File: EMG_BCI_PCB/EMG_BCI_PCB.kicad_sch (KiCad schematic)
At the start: 3 parts, among them J1 Conn_01x03, J2 Conn_01x02, J3 Conn_01x03_Male

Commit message: More schematic changes
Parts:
- removed J1: Conn_01x03, Connector_JST:JST_VH_B3P-VH_1x03_P3.96mm_Vertical, symbol Connector_Generic:Conn_01x03
- removed J2: Conn_01x02, Connector_JST:JST_XH_B2B-XH-AM_1x02_P2.50mm_Vertical, symbol Connector_Generic:Conn_01x02
- removed J3: Conn_01x03_Male, Connector_PinHeader_2.54mm:PinHeader_1x03_P2.54mm_Vertical, symbol Connector:Conn_01x03_Male
- added J1: Conn_01x08_Pin, symbol Connector:Conn_01x08_Pin
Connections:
- net EMG_FrontEnd/Trode+: now also J1.1 (Pin_1)
- net EMG_FrontEnd/Trode-: now also J1.2 (Pin_2)
- net Power/Vin+: now also J1.3 (Pin_3)
- new net Power/RTN: J1.4 (Pin_4)
- new net SpiClk: J1.5 (Pin_5)
- new net SpiCs: J1.8 (Pin_8)
- new net SpiDin: J1.6 (Pin_6)
- new net SpiDout: J1.7 (Pin_7)
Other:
- sheet EMG_Rect renamed EMG_Offset_And_Rect
- sheet EMG_ADC ports: added AdcCh0, AdcCh1, CLK, DIN, DOUT, ~{CS}/SHDN; removed ADDR, AN_0, AN_1, SCL, SDA
- sheet EMG_Offset_And_Rect ports: added RawSignalAdc, RectSignalAdc; removed AN_ADC
- sheet Power ports: added RTN; removed WGND

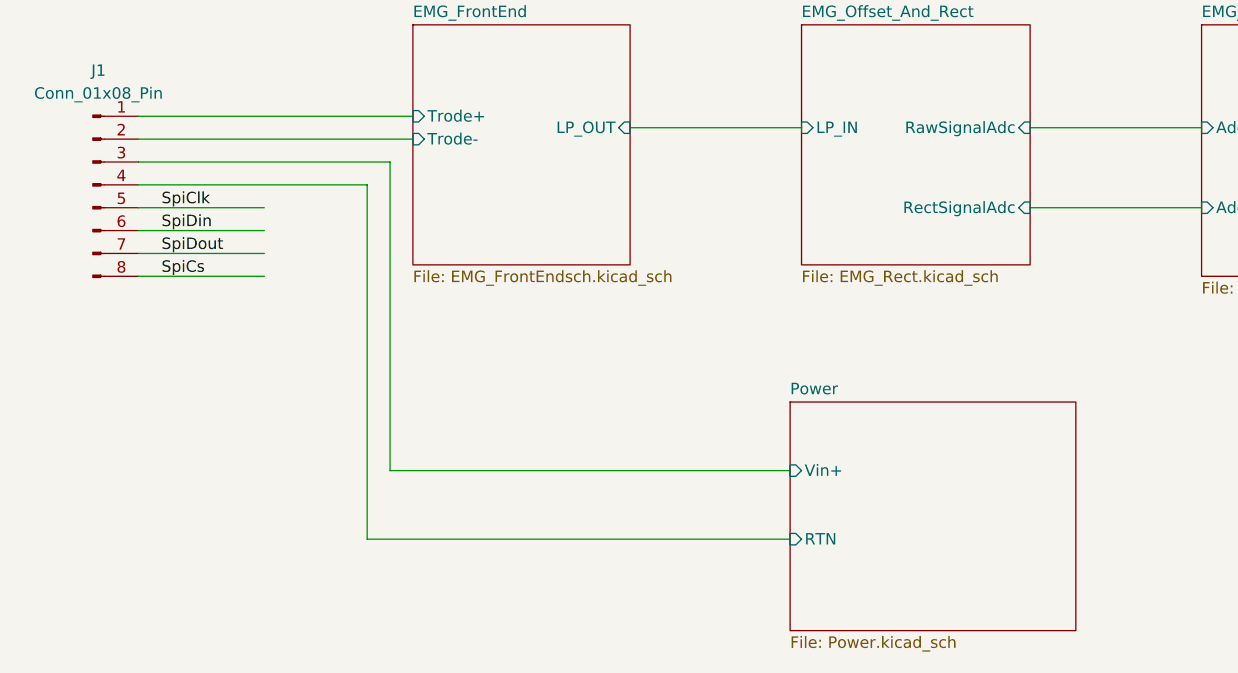
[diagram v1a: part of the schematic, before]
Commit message: Added power symbols for +/-3.3V
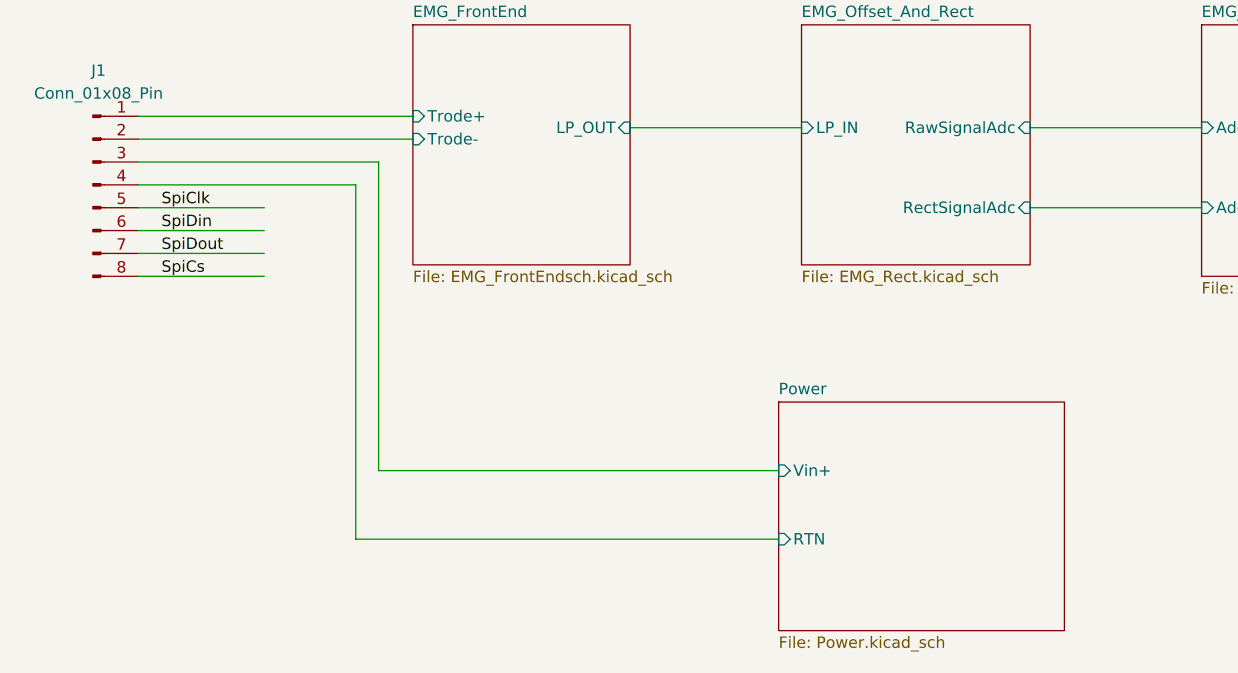
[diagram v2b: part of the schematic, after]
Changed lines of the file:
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@@
 	(wire
 		(pts
-			(xy 120.65 133.35) (xy 73.66 133.35)
+			(xy 119.38 133.35) (xy 72.39 133.35)
 		)
 		(stroke
@@
 	(wire
 		(pts
-			(xy 73.66 133.35) (xy 73.66 93.98)
+			(xy 72.39 133.35) (xy 72.39 93.98)
 		)
 		(stroke
@@
 	(wire
 		(pts
-			(xy 76.2 125.73) (xy 76.2 91.44)
-		)
-		(stroke
-			(width 0)
-			(type default)
-		)
-	)
-	(wire
-		(pts
-			(xy 73.66 93.98) (xy 48.26 93.98)
+			(xy 74.93 125.73) (xy 74.93 91.44)
+		)
+		(stroke
+			(width 0)
+			(type default)
+		)
+	)
+	(wire
+		(pts
+			(xy 72.39 93.98) (xy 48.26 93.98)
 		)
 		(stroke
@@
 	(wire
 		(pts
-			(xy 76.2 91.44) (xy 48.26 91.44)
+			(xy 74.93 91.44) (xy 48.26 91.44)
 		)
 		(stroke
@@
 	(wire
 		(pts
-			(xy 120.65 125.73) (xy 76.2 125.73)
+			(xy 119.38 125.73) (xy 74.93 125.73)
 		)
 		(stroke
@@
 	)
 	(sheet
-		(at 120.65 118.11)
+		(at 119.38 118.11)
 		(size 31.75 25.4)
 		(exclude_from_sim no)
@@
 		)
 		(property "Sheetname" "Power"
-			(at 120.65 117.3984 0)
+			(at 119.38 117.3984 0)
 			(effects
 				(font
@@
 		)
 		(property "Sheetfile" "Power.kicad_sch"
-			(at 120.65 144.0946 0)
+			(at 119.38 144.0946 0)
 			(effects
 				(font
@@
 		)
 		(pin "RTN" input
-			(at 120.65 133.35 180)
+			(at 119.38 133.35 180)
 			(effects
 				(font
@@
 		)
 		(pin "Vin+" input
-			(at 120.65 125.73 180)
-			(effects
-				(font
+			(at 119.38 125.73 180)
+			(effects
+				(font

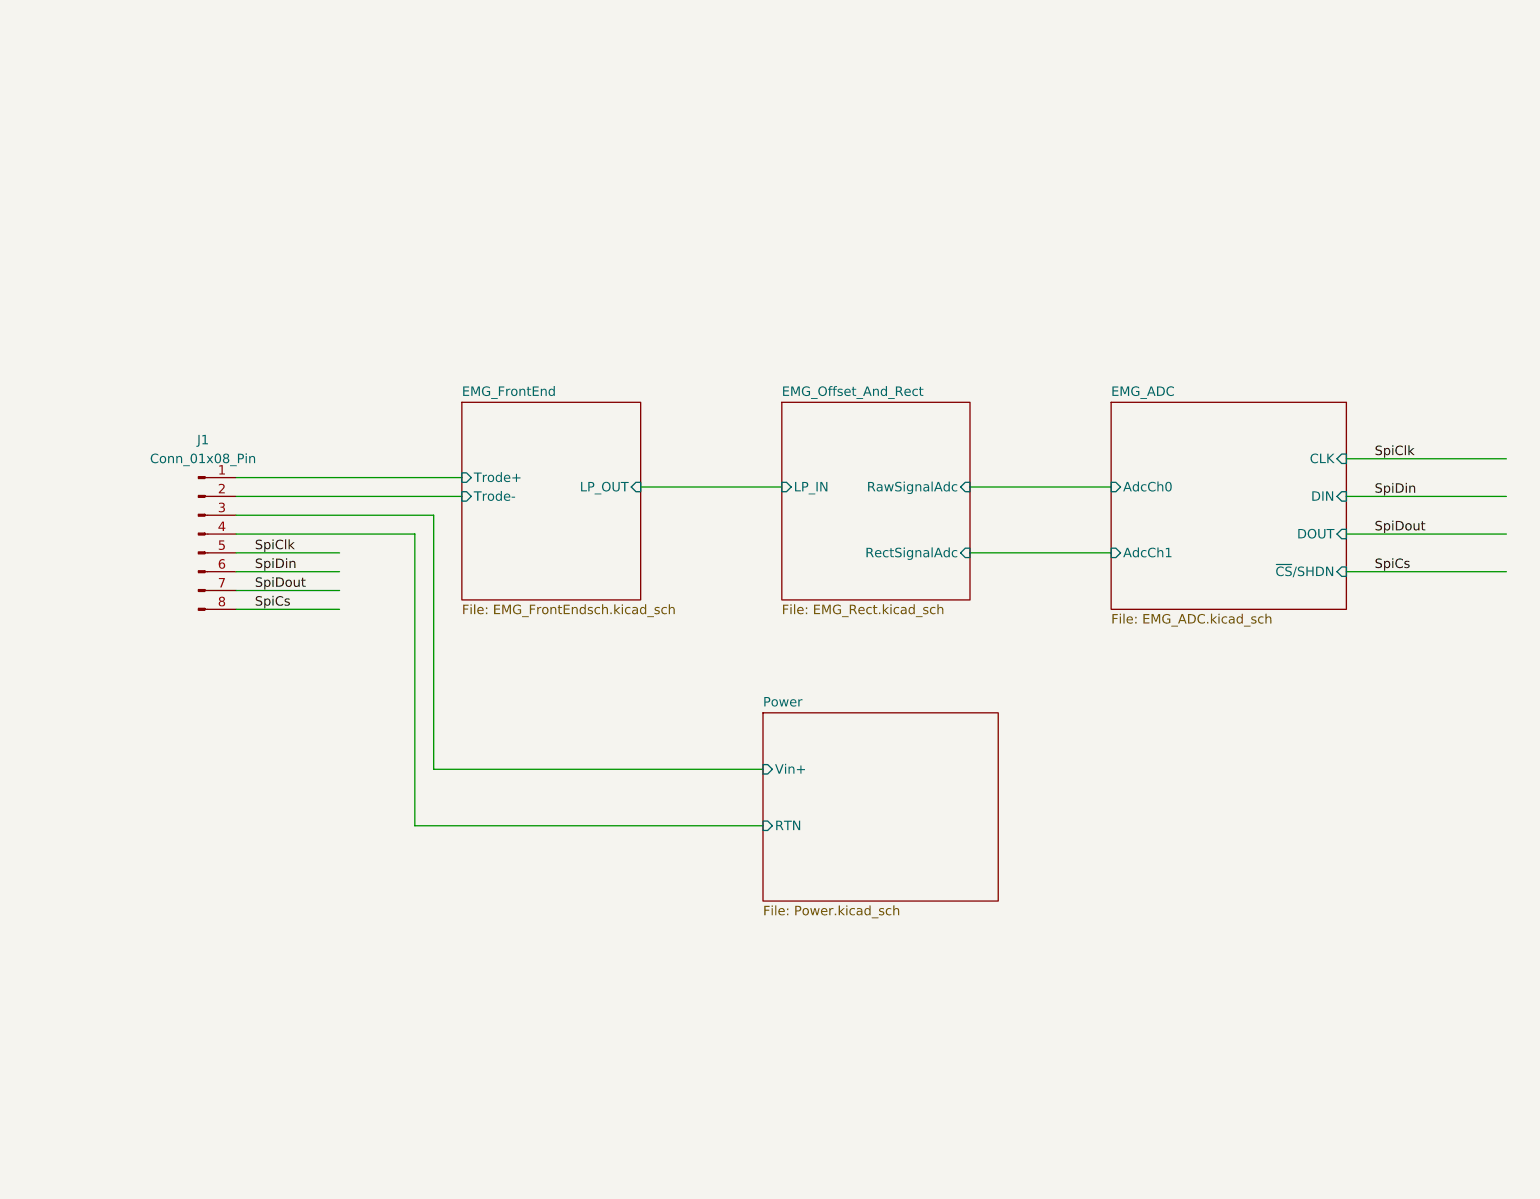
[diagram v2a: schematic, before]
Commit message: Removed some warnings from the electrical rules
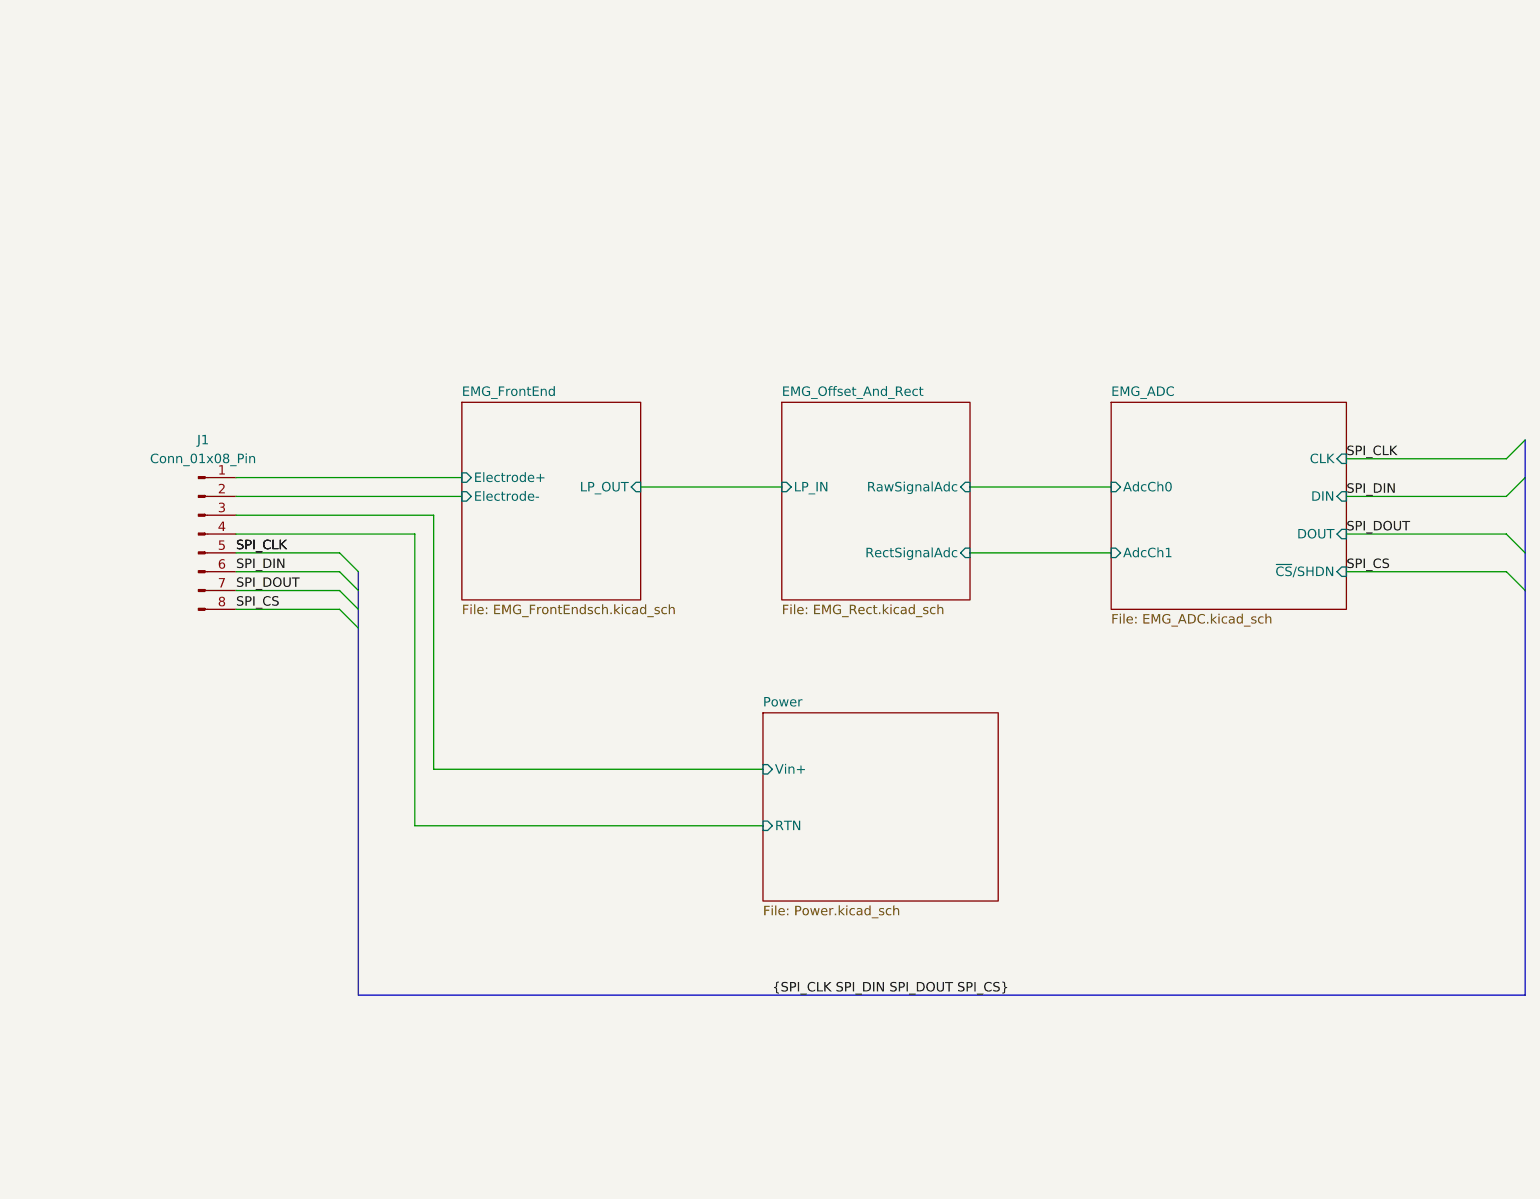
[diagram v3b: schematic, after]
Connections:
- net EMG_FrontEnd/Trode+ renamed EMG_FrontEnd/Electrode+
- net EMG_FrontEnd/Trode- renamed EMG_FrontEnd/Electrode-
- net SpiClk renamed SPI_CLK
- net SpiCs renamed SPI_CS
- net SpiDin renamed SPI_DIN
- net SpiDout renamed SPI_DOUT
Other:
- sheet EMG_FrontEnd ports: added Electrode+, Electrode-; removed Trode+, Trode-

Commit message: finally assigned the footprints to the schematic symbols
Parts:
- J1: footprint (none) -> Connector_PinSocket_2.54mm:PinSocket_1x08_P2.54mm_Vertical_SMD_Pin1Right
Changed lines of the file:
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@@
 			)
 		)
-		(property "Footprint" ""
+		(property "Footprint" "Connector_PinSocket_2.54mm:PinSocket_1x08_P2.54mm_Vertical_SMD_Pin1Right"
 			(at 43.18 93.98 0)
 			(effects

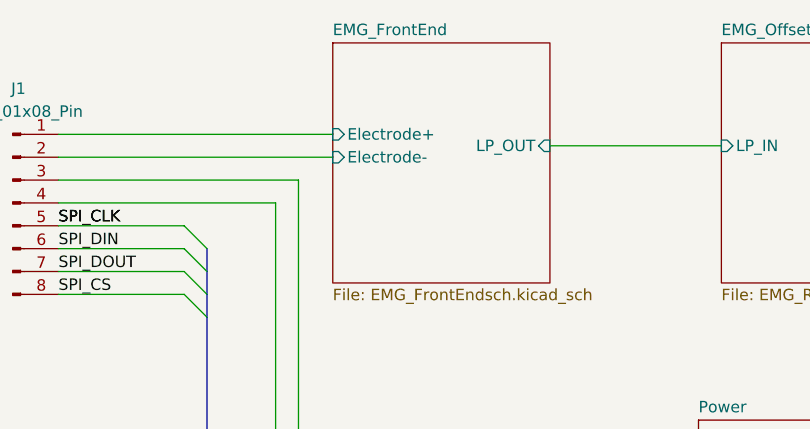
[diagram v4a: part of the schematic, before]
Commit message: Initial placement and routing
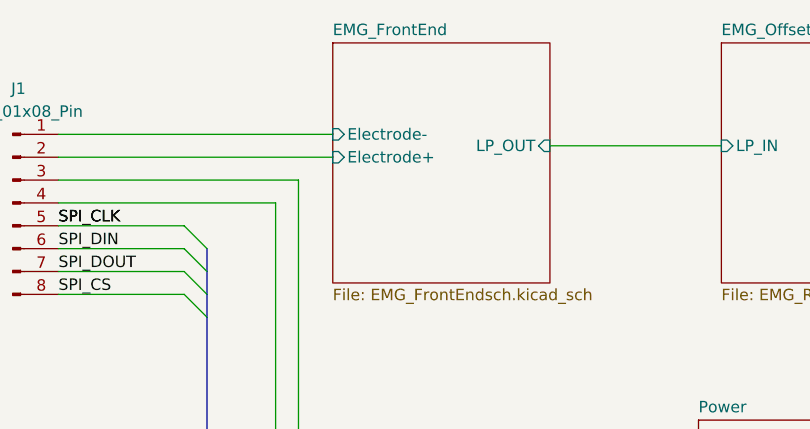
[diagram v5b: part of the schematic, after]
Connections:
- net EMG_FrontEnd/Electrode+: now also J1.2 (Pin_2); no longer J1.1 (Pin_1)
- net EMG_FrontEnd/Electrode-: now also J1.1 (Pin_1); no longer J1.2 (Pin_2)
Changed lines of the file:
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@@
+	(wire
+		(pts
+			(xy 119.38 133.35) (xy 72.39 133.35)
+		)
+		(stroke
+			(width 0)
+			(type default)
+		)
+	)
+	(bus
+		(pts
+			(xy 222.25 101.6) (xy 222.25 156.21)
+		)
+		(stroke
+			(width 0)
+			(type default)
+		)
+	)
+	(wire
+		(pts
+			(xy 72.39 133.35) (xy 72.39 93.98)
+		)
+		(stroke
+			(width 0)
+			(type default)
+		)
+	)
+	(wire
+		(pts
+			(xy 48.26 96.52) (xy 62.23 96.52)
+		)
+		(stroke
+			(width 0)
+			(type default)
+		)
+	)
+	(wire
+		(pts
+			(xy 74.93 125.73) (xy 74.93 91.44)
+		)
+		(stroke
+			(width 0)
+			(type default)
+		)
+	)
+	(wire
+		(pts
+			(xy 48.26 104.14) (xy 62.23 104.14)
+		)
+		(stroke
+			(width 0)
+			(type default)
+		)
+	)
+	(wire
+		(pts
+			(xy 62.23 101.6) (xy 48.26 101.6)
+		)
+		(stroke
+			(width 0)
+			(type default)
+		)
+	)
+	(wire
+		(pts
+			(xy 219.71 93.98) (xy 198.12 93.98)
+		)
+		(stroke
+			(width 0)
+			(type default)
+		)
+	)
+	(wire
+		(pts
+			(xy 48.26 86.36) (xy 78.74 86.36)
+		)
+		(stroke
+			(width 0)
+			(type default)
+		)
+	)
+	(wire
+		(pts
+			(xy 72.39 93.98) (xy 48.26 93.98)
+		)
+		(stroke
+			(width 0)
+			(type default)
+		)
+	)
 	(wire
 		(pts
 			(xy 48.26 88.9) (xy 78.74 88.9)
-		)
-		(stroke
-			(width 0)
-			(type default)
-		)
-	)
-	(wire
-		(pts
-			(xy 119.38 133.35) (xy 72.39 133.35)
-		)
-		(stroke
-			(width 0)
-			(type default)
-		)
-	)
-	(bus
-		(pts
-			(xy 222.25 101.6) (xy 222.25 156.21)
-		)
-		(stroke
-			(width 0)
-			(type default)
-		)
-	)
-	(wire
-		(pts
-			(xy 72.39 133.35) (xy 72.39 93.98)
-		)
-		(stroke
-			(width 0)
-			(type default)
-		)
-	)
-	(wire
-		(pts
-			(xy 48.26 86.36) (xy 78.74 86.36)
-		)
-		(stroke
-			(width 0)
-			(type default)
-		)
-	)
-	(wire
-		(pts
-			(xy 48.26 96.52) (xy 62.23 96.52)
-		)
-		(stroke
-			(width 0)
-			(type default)
-		)
-	)
-	(wire
-		(pts
-			(xy 74.93 125.73) (xy 74.93 91.44)
-		)
-		(stroke
-			(width 0)
-			(type default)
-		)
-	)
-	(wire
-		(pts
-			(xy 48.26 104.14) (xy 62.23 104.14)
-		)
-		(stroke
-			(width 0)
-			(type default)
-		)
-	)
-	(wire
-		(pts
-			(xy 62.23 101.6) (xy 48.26 101.6)
-		)
-		(stroke
-			(width 0)
-			(type default)
-		)
-	)
-	(wire
-		(pts
-			(xy 219.71 93.98) (xy 198.12 93.98)
-		)
-		(stroke
-			(width 0)
-			(type default)
-		)
-	)
-	(wire
-		(pts
-			(xy 72.39 93.98) (xy 48.26 93.98)
 		)
 		(stroke
@@
 		)
 		(pin "Electrode+" input
+			(at 78.74 88.9 180)
+			(effects
+				(font
+					(size 1.27 1.27)
+				)
+				(justify left)
+			)
+		)
+		(pin "Electrode-" input
 			(at 78.74 86.36 180)
 			(effects
 				(font
-					(size 1.27 1.27)
-				)
-				(justify left)
-			)
-		)
-		(pin "Electrode-" input
-			(at 78.74 88.9 180)
-			(effects
-				(font
